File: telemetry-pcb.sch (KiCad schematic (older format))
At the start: 35 parts, among them SW1 CAN_TERM

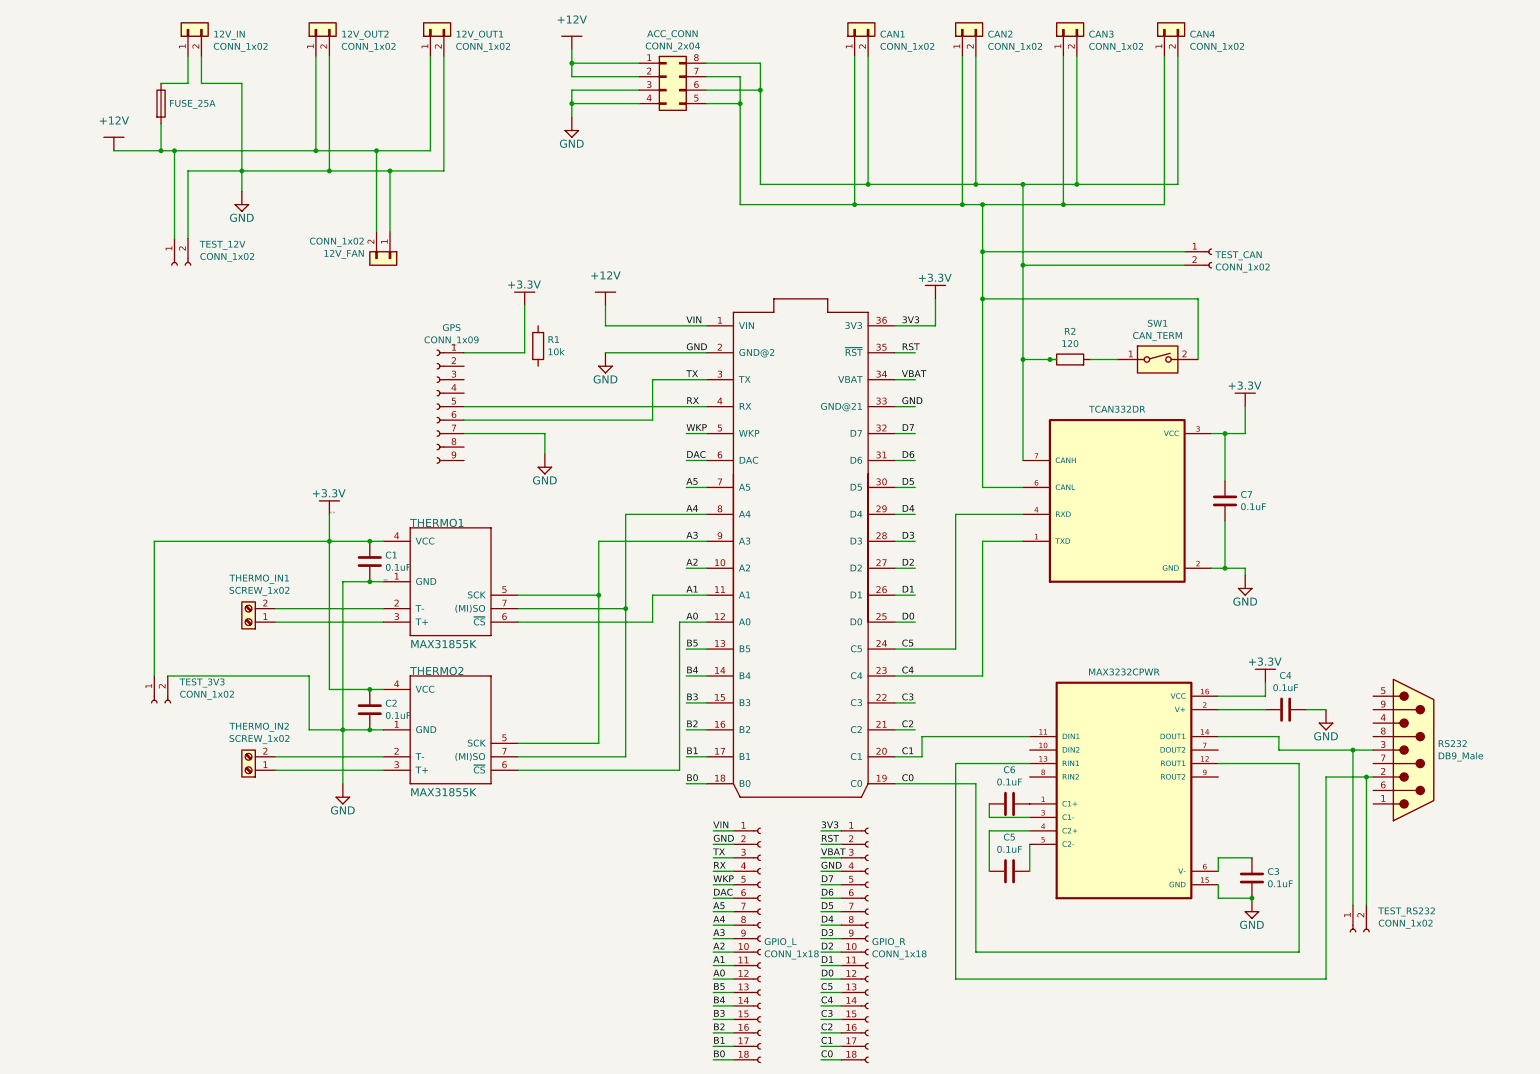
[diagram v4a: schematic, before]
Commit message: added first draft of BOM
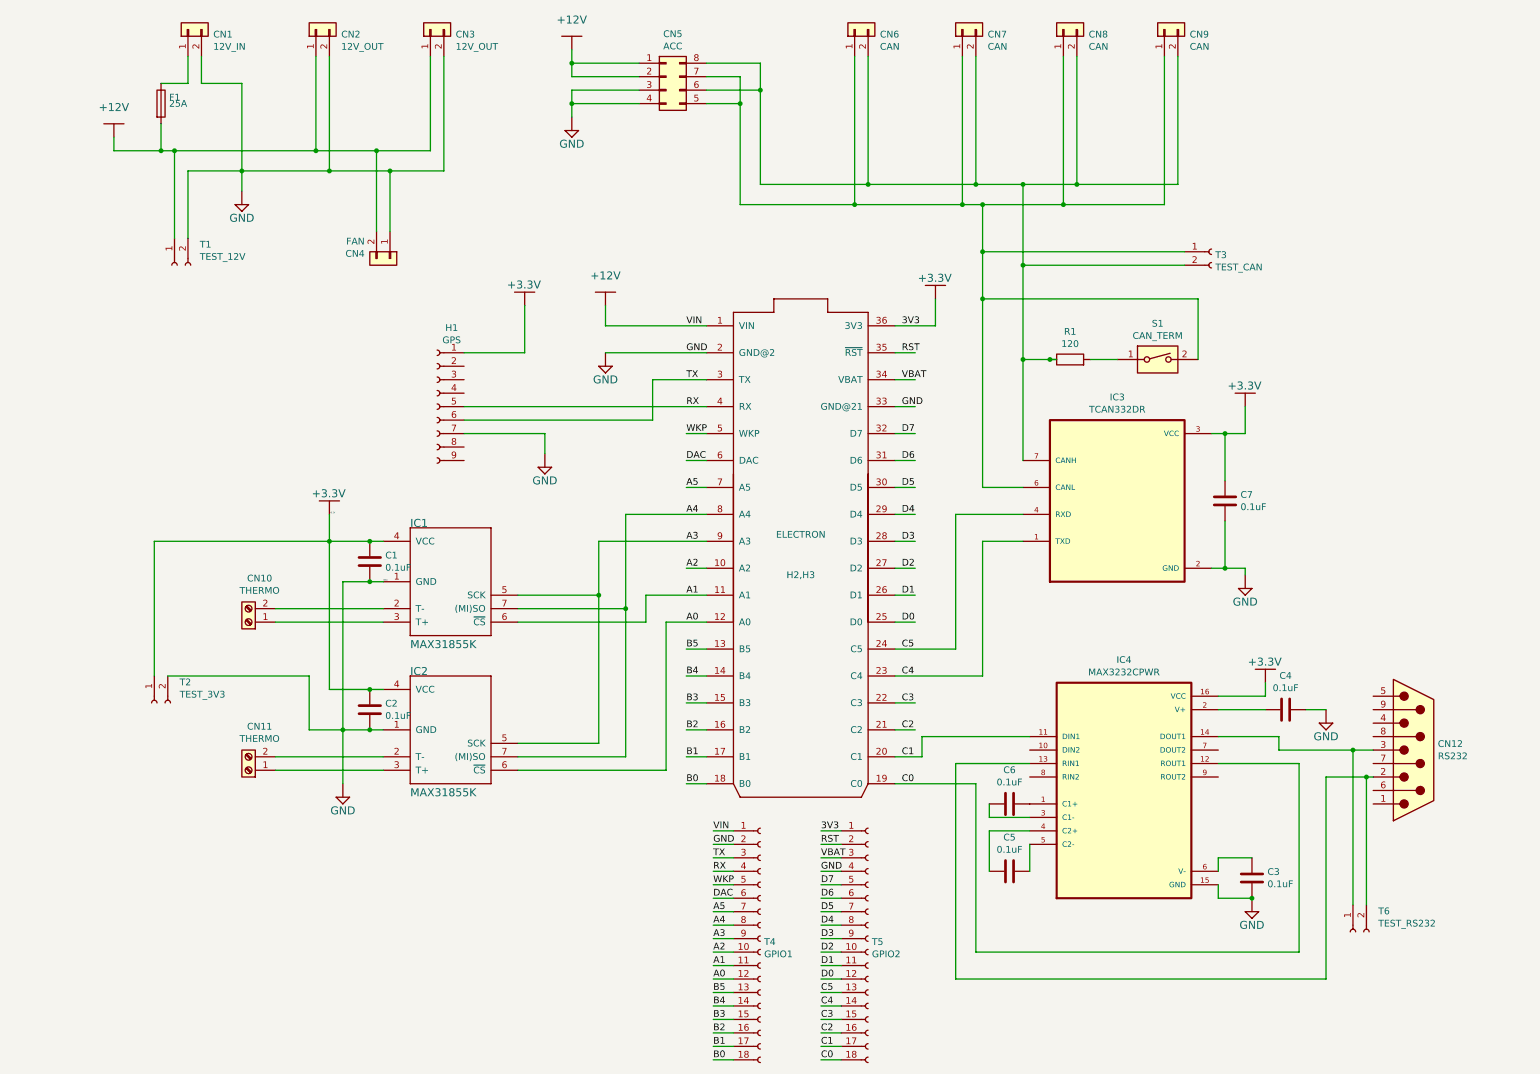
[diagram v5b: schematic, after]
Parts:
- removed R1: 10k, symbol Device:R
- CN1: renamed from 12V_IN; value CONN_1x02 -> 12V_IN
- CN10: renamed from THERMO_IN1; value SCREW_1x02 -> THERMO
- CN11: renamed from THERMO_IN2; value SCREW_1x02 -> THERMO
- CN12: renamed from RS232; value DB9_Male -> RS232
- CN2: renamed from 12V_OUT2; value CONN_1x02 -> 12V_OUT
- CN3: renamed from 12V_OUT1; value CONN_1x02 -> 12V_OUT
- CN4: renamed from 12V_FAN; value CONN_1x02 -> FAN
- CN5: renamed from ACC_CONN; value CONN_2x04 -> ACC
- CN6: renamed from CAN1; value CONN_1x02 -> CAN
- CN7: renamed from CAN2; value CONN_1x02 -> CAN
- CN8: renamed from CAN3; value CONN_1x02 -> CAN
- CN9: renamed from CAN4; value CONN_1x02 -> CAN
- F1: renamed from F?; value FUSE_25A -> 25A
- H1: renamed from GPS; value CONN_1x09 -> GPS
- H2,H3: renamed from U$1; value ELECTRON_WITH_HEADERS -> ELECTRON
- T1: renamed from TEST_12V; value CONN_1x02 -> TEST_12V
- T2: renamed from TEST_3V3; value CONN_1x02 -> TEST_3V3
- T3: renamed from TEST_CAN; value CONN_1x02 -> TEST_CAN
- T4: renamed from GPIO_L; value CONN_1x18 -> GPIO1
- T5: renamed from GPIO_R; value CONN_1x18 -> GPIO2
- T6: renamed from TEST_RS232; value CONN_1x02 -> TEST_RS232
- gave numbers to parts that had none: 2
- renumbered THERMO1 to IC1, THERMO2 to IC2, R2 to R1, SW1 to S1
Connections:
- wire segments 228 -> 229

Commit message: fixed design rule violations and added input diode
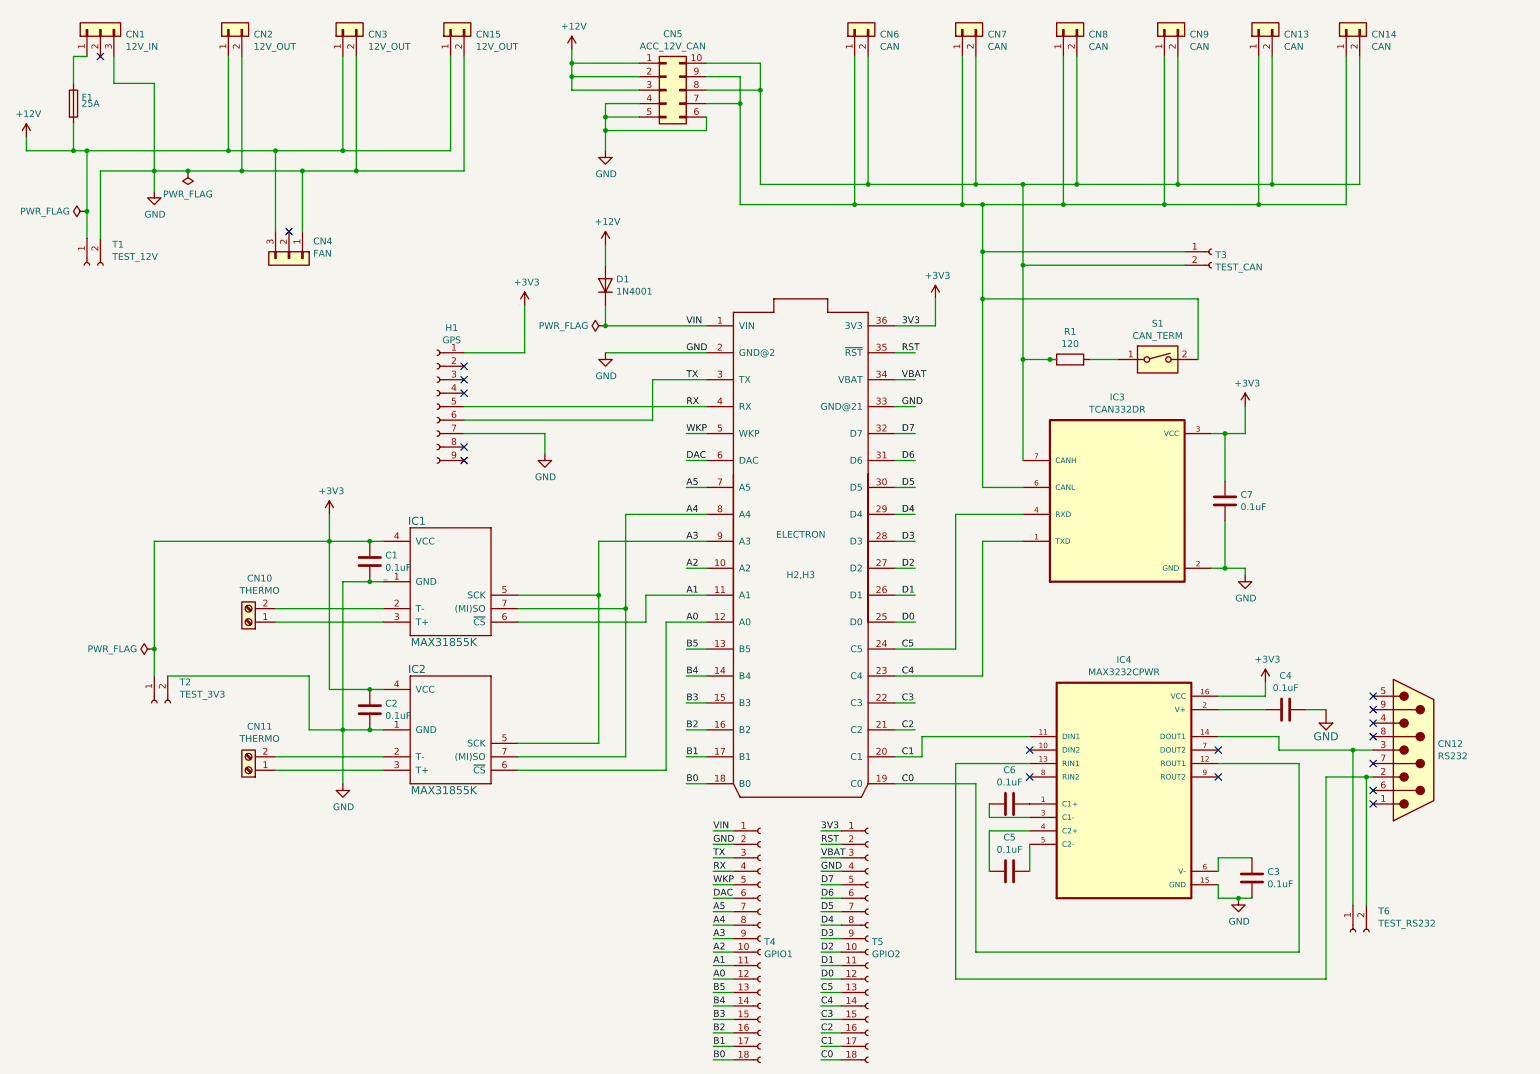
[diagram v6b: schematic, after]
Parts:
- removed CN1: 12V_IN, symbol Connector_Generic:Conn_01x02
- removed CN4: FAN, symbol Connector_Generic:Conn_01x02
- removed CN5: ACC, symbol Connector_Generic:Conn_02x04_Counter_Clockwise
- added CN1: 12V_IN, symbol Connector_Generic:Conn_01x03
- added CN13, CN14: CAN, symbol Connector_Generic:Conn_01x02
- added CN15: 12V_OUT, symbol Connector_Generic:Conn_01x02
- added CN4: FAN, symbol Connector_Generic:Conn_01x03
- added CN5: ACC_12V_CAN, symbol Connector_Generic:Conn_02x05_Counter_Clockwise
- added D1: 1N4001, symbol Device:D
- IC1, IC2: footprint telemetry-pcb:SO08 -> (none)
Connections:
- net labels added: +3V3
- net labels removed: +3.3V
- wire segments 229 -> 251
- no-connect marks 0 -> 18
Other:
- moved on the sheet: CN2, CN3, F1, T1

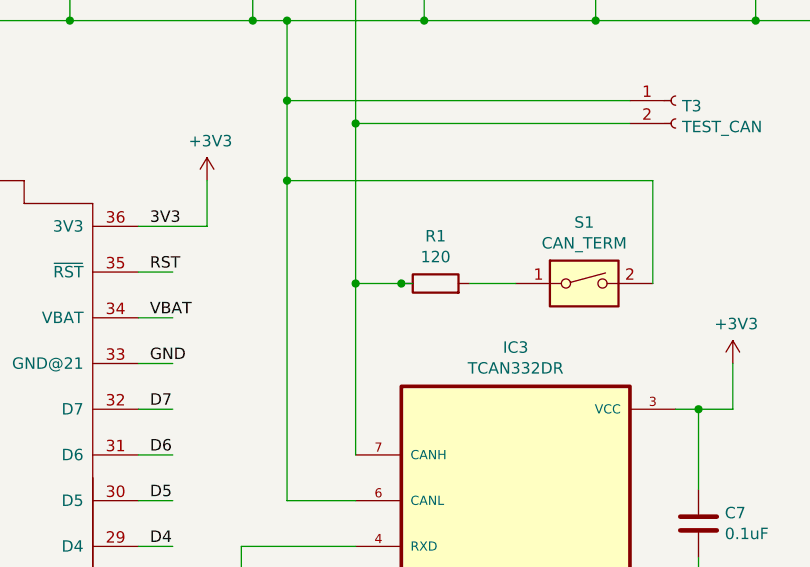
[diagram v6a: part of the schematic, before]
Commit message: removed trailing wire under R1
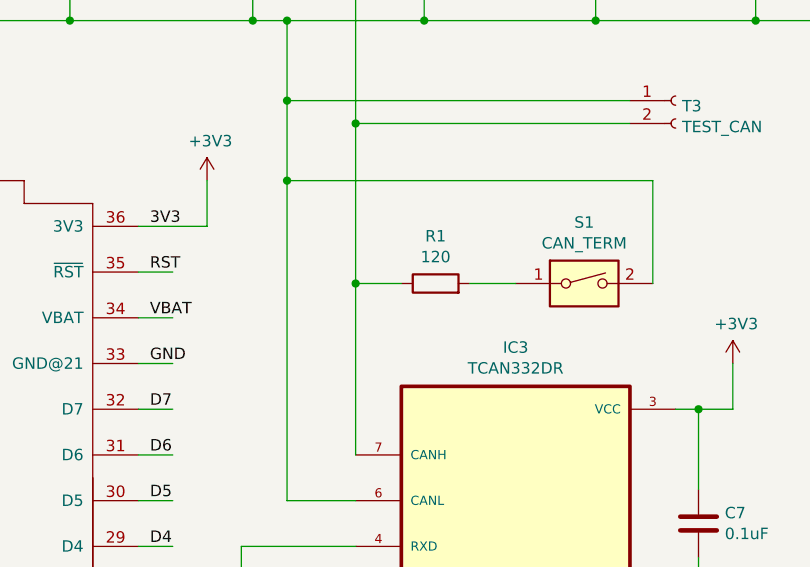
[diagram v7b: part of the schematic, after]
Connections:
- wire segments 251 -> 250
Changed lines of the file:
@@
 Wire Wire Line
 	7750 2300 9350 2300
-Connection ~ 8250 2750
-Wire Wire Line
-	8250 2750 8300 2750
 Wire Wire Line
 	8550 2750 8750 2750

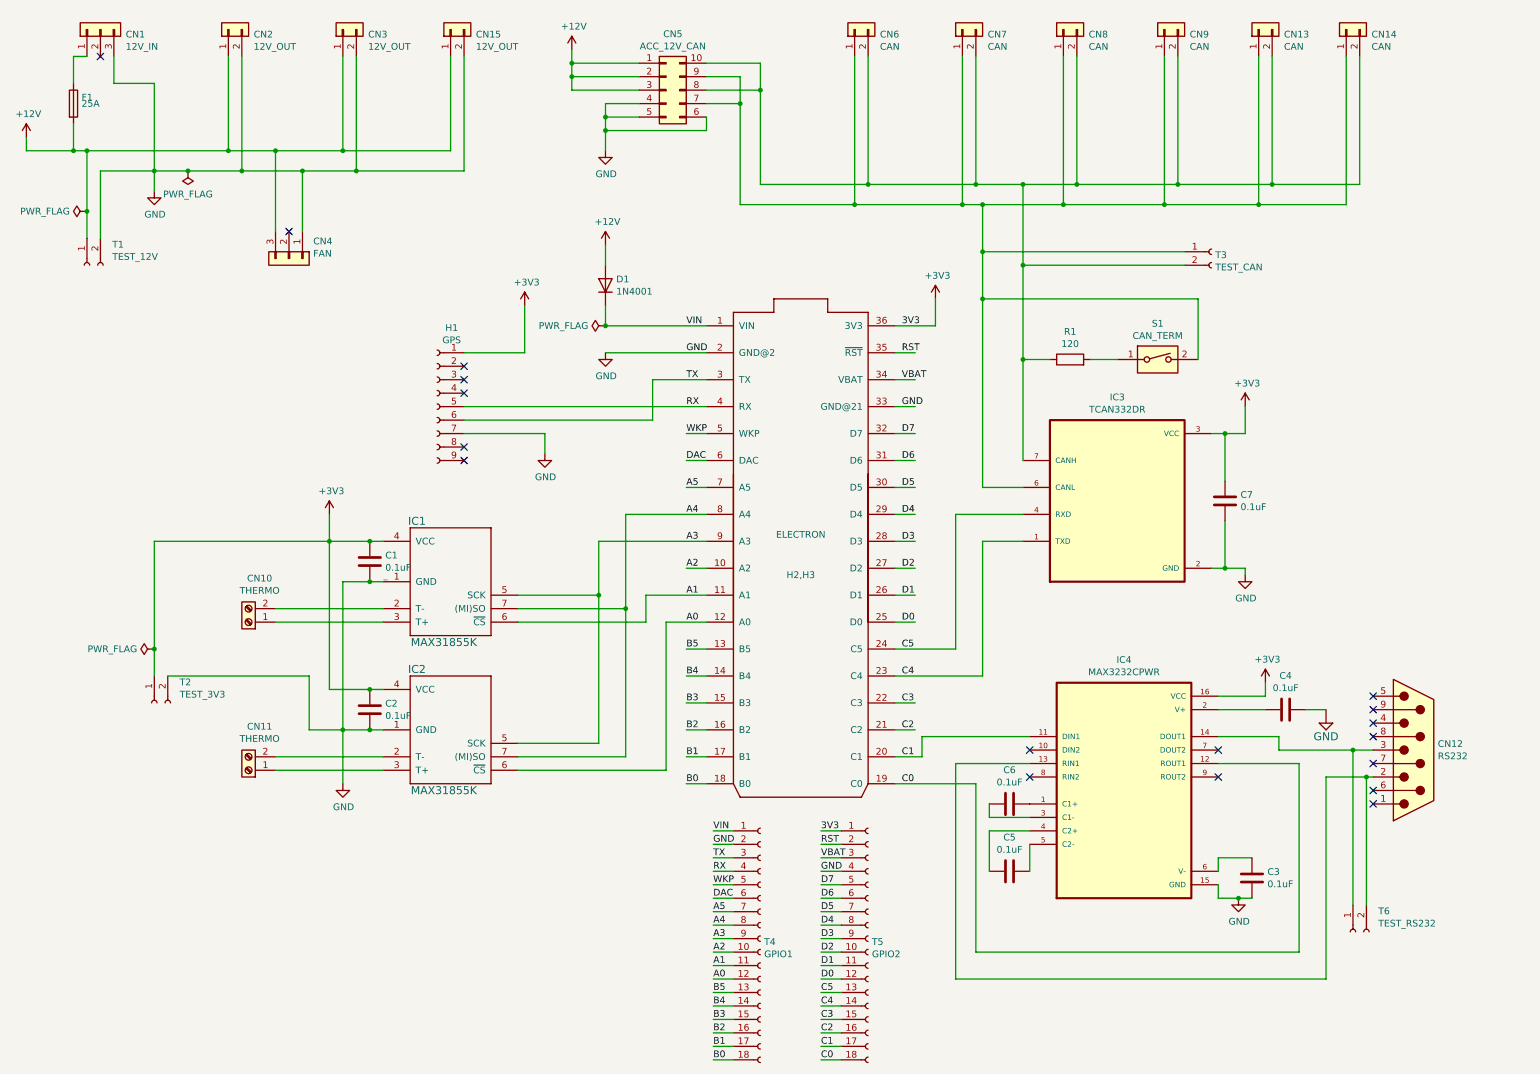
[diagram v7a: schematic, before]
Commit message: finalized schematic based on review feedback
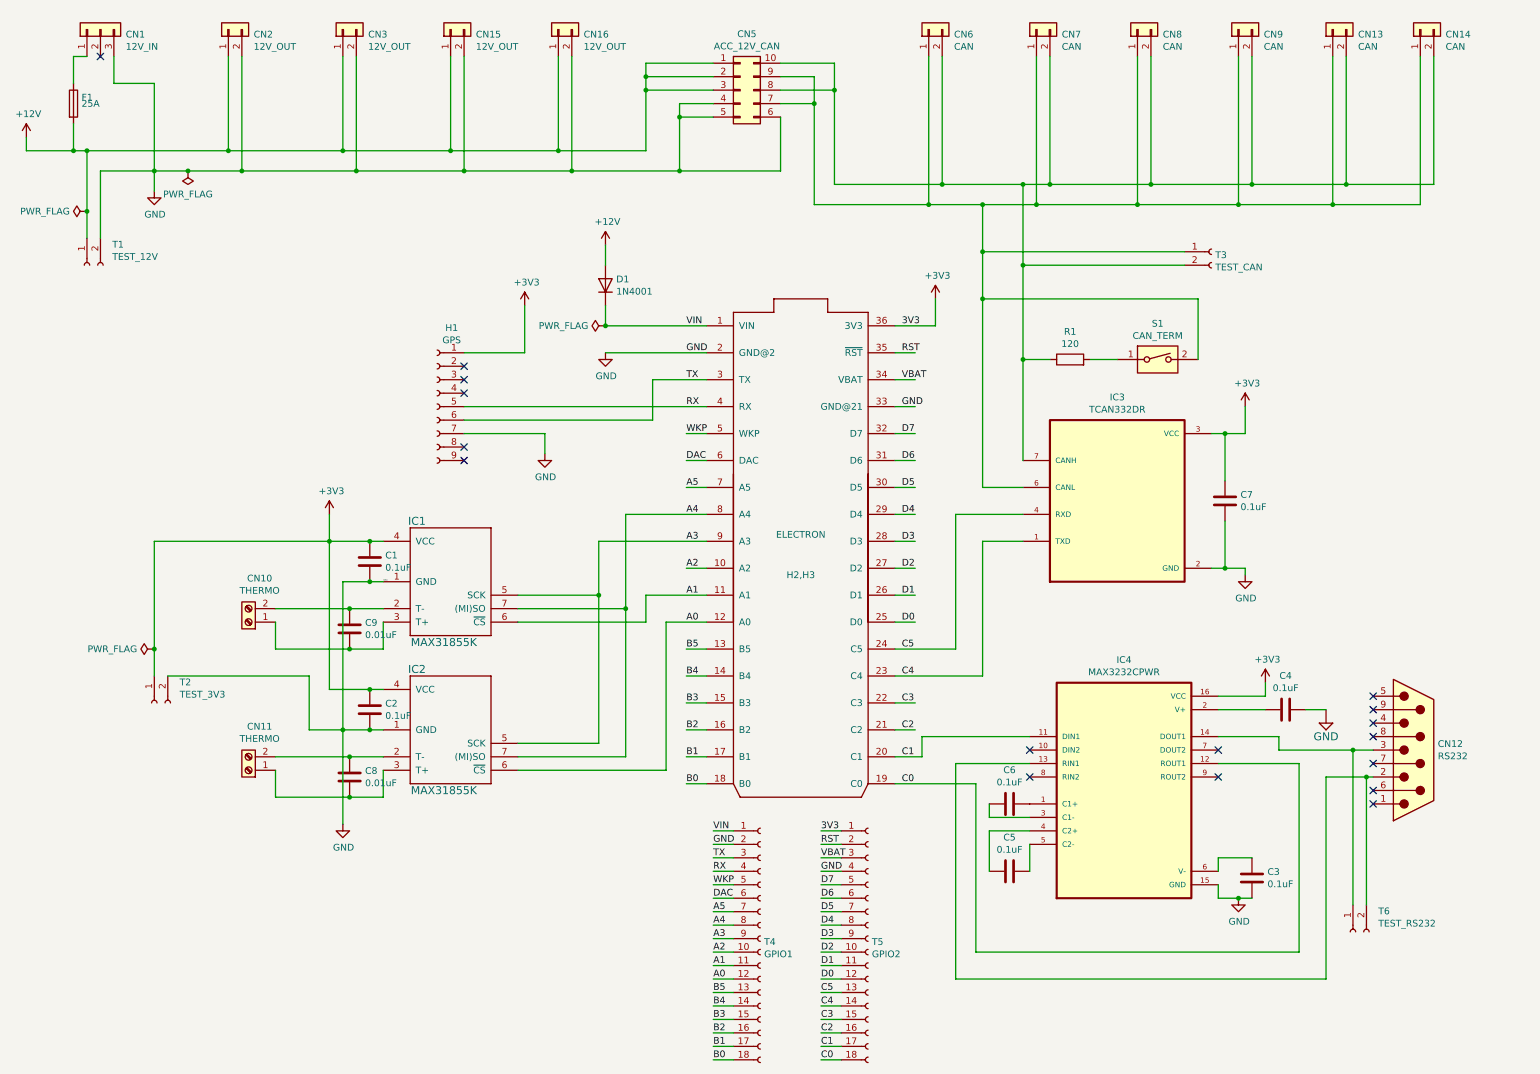
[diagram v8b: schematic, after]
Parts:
- removed CN4: FAN, symbol Connector_Generic:Conn_01x03
- added C8, C9: 0.01uF, symbol Device:C
- added CN16: 12V_OUT, symbol Connector_Generic:Conn_01x02
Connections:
- wire segments 250 -> 259
- no-connect marks 18 -> 17
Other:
- moved on the sheet: CN13, CN14, CN5, CN6, CN7, CN8, CN9
